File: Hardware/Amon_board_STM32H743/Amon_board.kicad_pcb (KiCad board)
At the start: 4 copper layers, 70 x 120 mm, 262 parts, among them J1 USB_C_Receptacle_USB2.0, J10 GTFP08131Y2HR, J11 Conn_01x03_Male, J13 Conn_01x04_Male, J14 Conn_01x04_Male, J15 Conn_01x06_Male, J16 XT60PW-M20, J17 XT60PW-M20, J18 SMA Edge, J19 SMA Edge, J2 Conn_01x04_Pin, J3 Conn_01x04_Pin, J4 HAB-VCR-010-LF, J5 Conn_01x04_Pin, J7 Red leds, J8 White leds, J9 AUX, M1 Servo_X+, M2 Servo_X-, M3 Servo_Y+, M4 Servo_Y-, Q1 BC817, Q2 BC817, Q3 BC817, Q6 BC817, Q7 AO3401A, Q8 BC817, Q9 AO3401A, SW3 SW_SPST, U10 NRF24L01, U11 NRF24L01, U12 RFX2401C, U13 RFX2401C, U14 CH340G, U15 MP2303ADN, U3 W25Q128JVS, U4 MP2303ADN, U5 MP2303ADN, U6 MPU-6050, U7 BME280, U8 HMC5883L, U9 STM32H743VIT6, Y1 48MHz, Y2 32.768kHz, Y3 16MHz, Y4 16MHz, Y5 12MHz

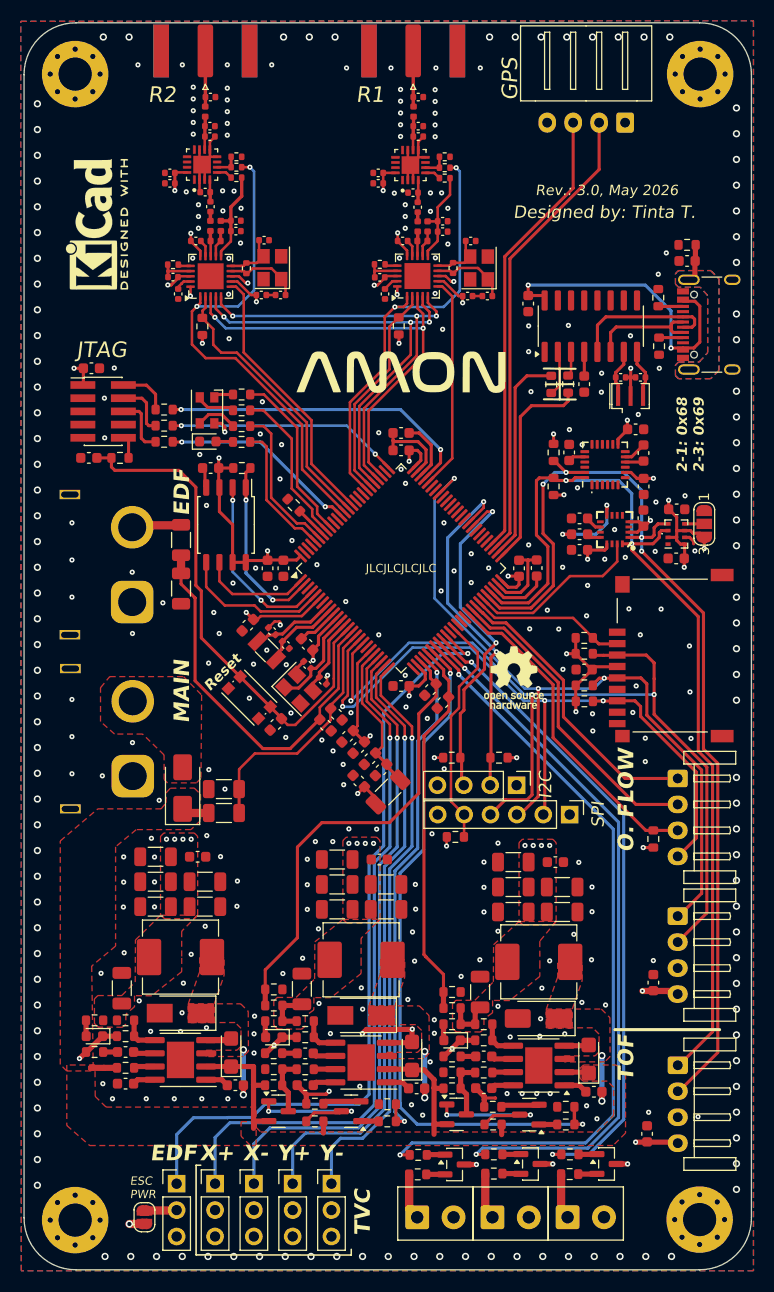
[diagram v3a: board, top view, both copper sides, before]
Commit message: Update: finished PCB v3, gerbers, ordered board, readme update
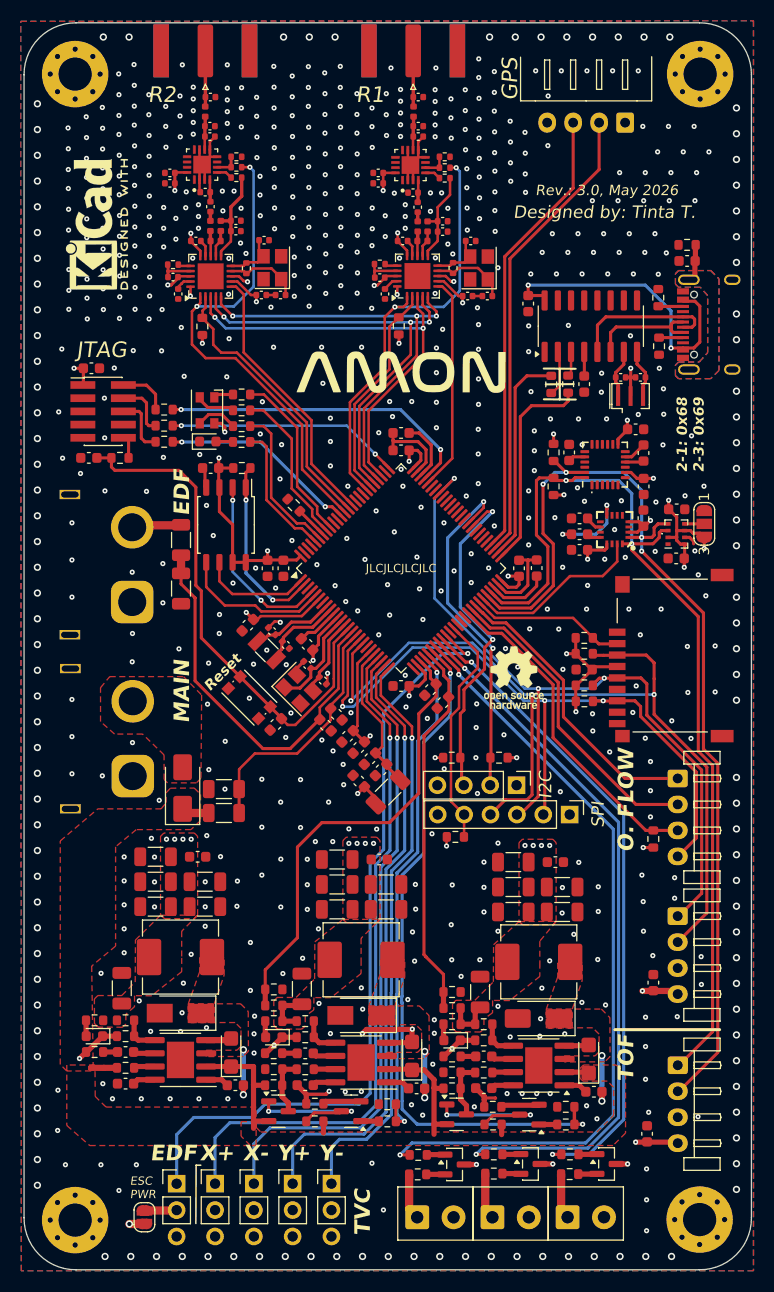
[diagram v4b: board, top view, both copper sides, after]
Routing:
- net GND: track 102.2 -> 102.1 mm, vias 369 -> 747
